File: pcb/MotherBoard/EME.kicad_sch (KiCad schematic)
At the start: 58 parts, among them J1 BMP180, J10 Reset, J11 UART2, J12 SPI_CONN, J13 UART0, J14 GPIO's, J17 Anemómetro, J19 I2C, J2 volti, J20 Jumper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

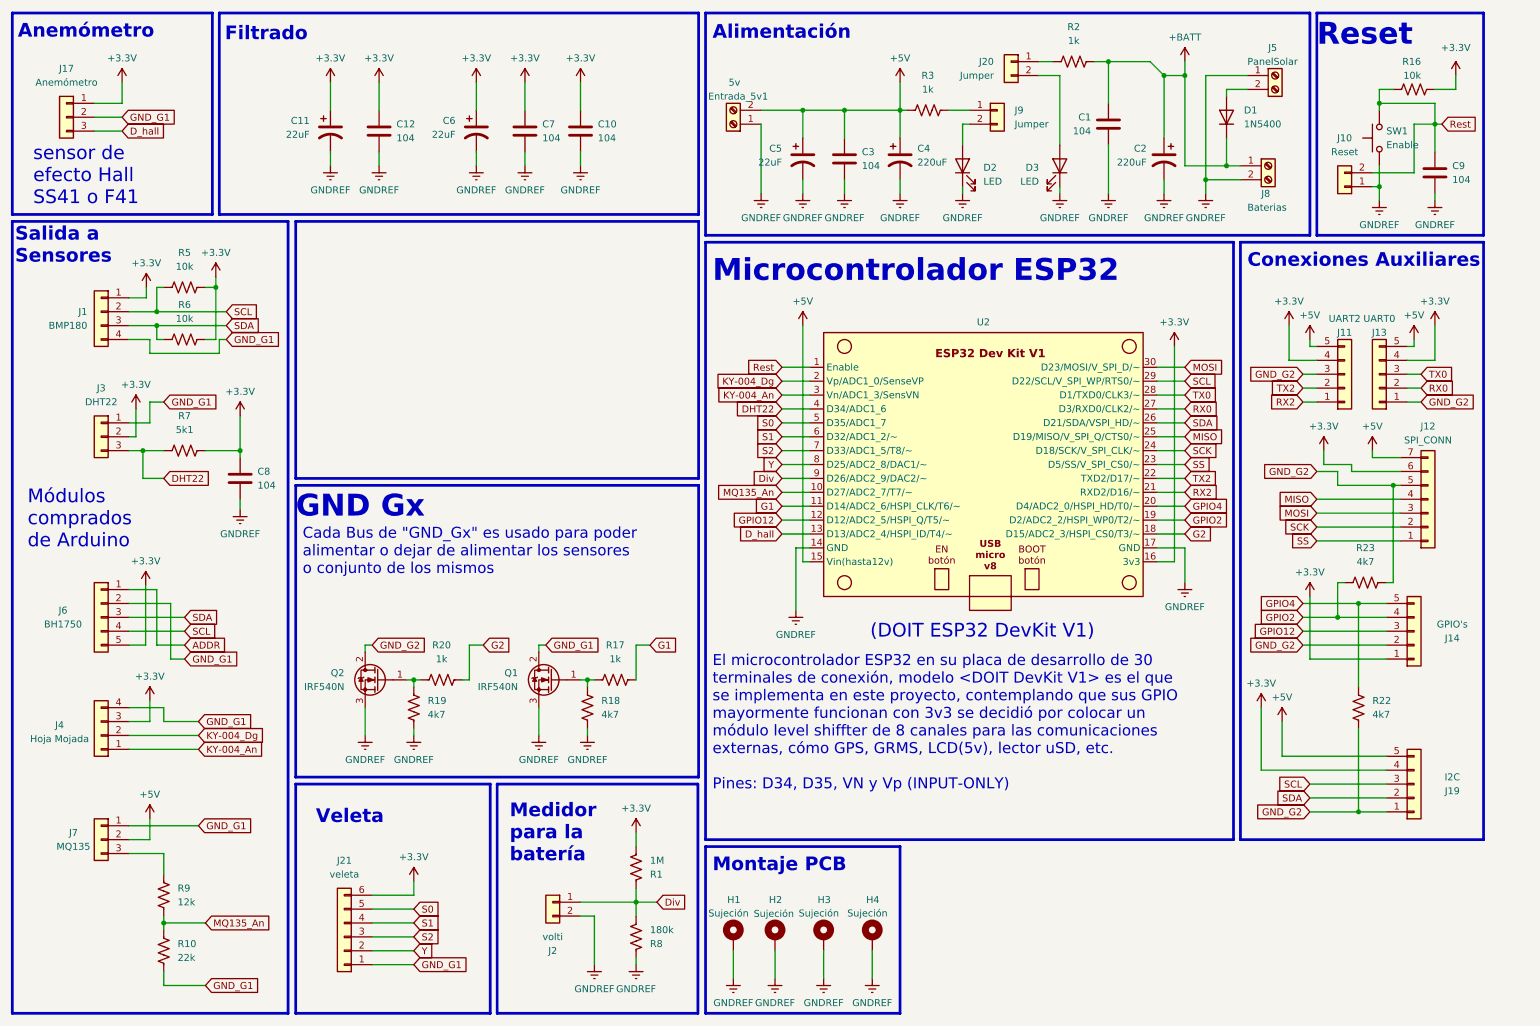
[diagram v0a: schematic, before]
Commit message: "se modificó conexión del DHT22 a otro pin, se agregó jumper G-g1 y g2, también conectores para extraer alimentación"
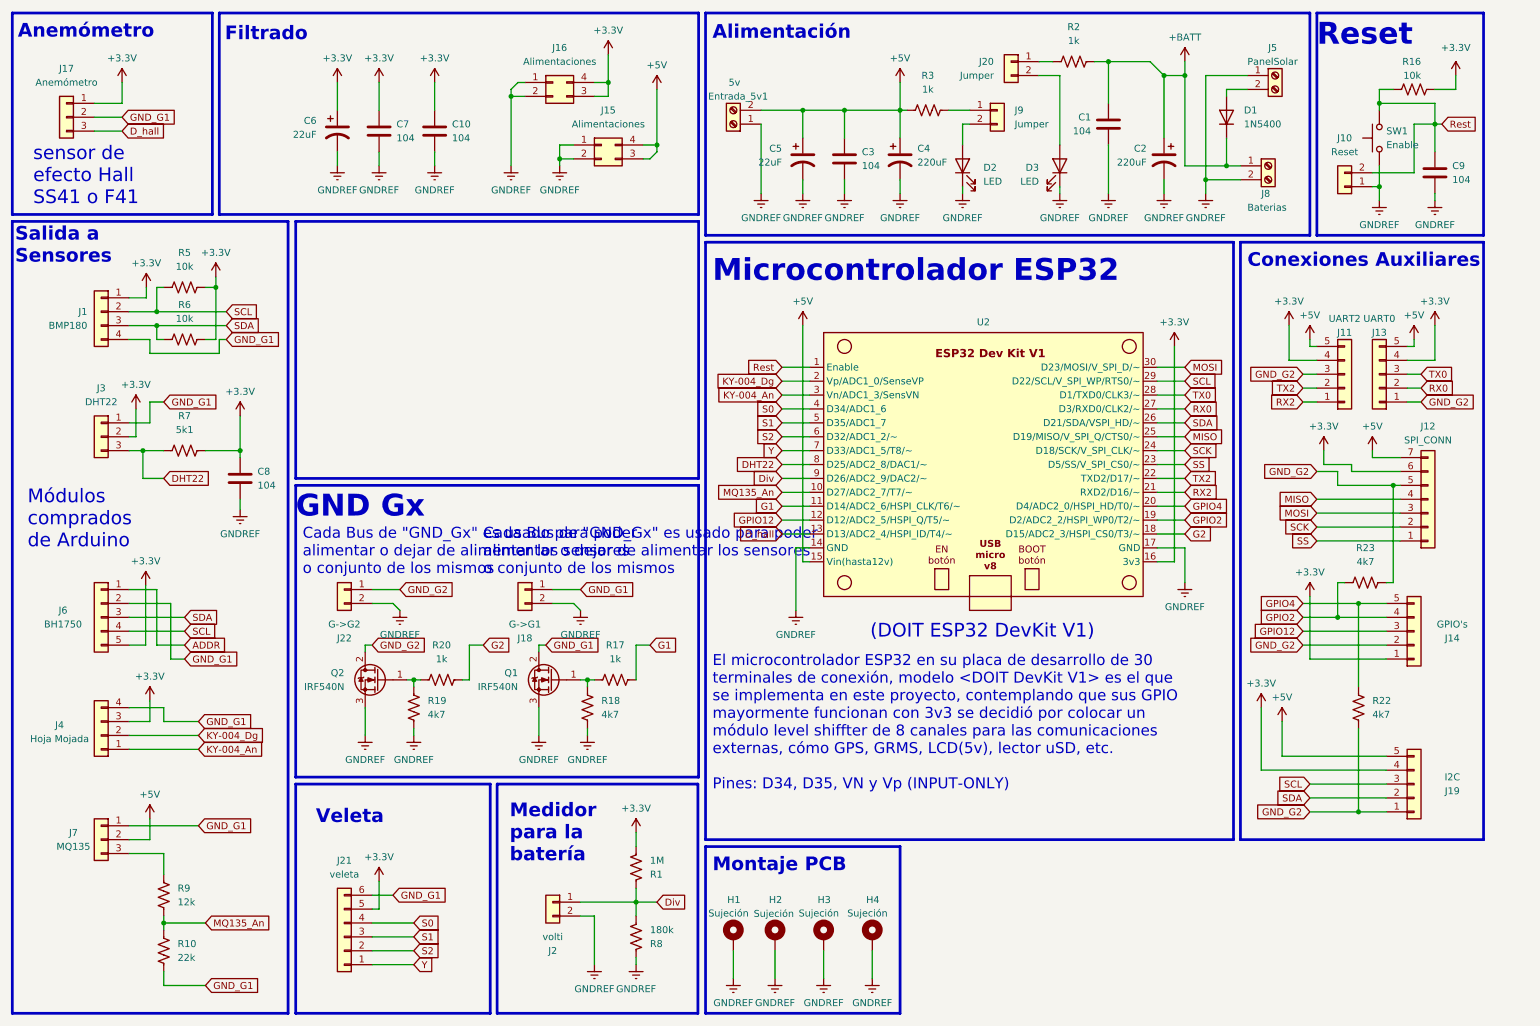
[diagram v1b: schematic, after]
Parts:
- removed C11: 22uF, Capacitor_THT:C_Radial_D8.0mm_H7.0mm_P3.50mm, symbol Device:C_Polarized_US
- removed C12: 104, Capacitor_THT:C_Disc_D7.0mm_W2.5mm_P5.00mm, symbol Device:C
- added J15, J16: Alimentaciones, Connector_PinHeader_2.54mm:PinHeader_2x02_P2.54mm_Vertical, symbol Connector_Generic:Conn_02x02_Counter_Clockwise
- added J18: G->G1, Connector_PinHeader_2.54mm:PinHeader_1x02_P2.54mm_Vertical, symbol Connector_Generic:Conn_01x02
- added J22: G->G2, Connector_PinHeader_2.54mm:PinHeader_1x02_P2.54mm_Vertical, symbol Connector_Generic:Conn_01x02
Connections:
- net +3.3V: now also J21.5 (Pin_5), J16.3 (Pin_3), J16.4 (Pin_4); no longer J21.6 (Pin_6)
- net +5V: now also J15.3 (Pin_3), J15.4 (Pin_4)
- net DHT22: now also U2.8 (D25/ADC2_8/DAC1/~); no longer U2.4 (D34/ADC1_6)
- net GNDREF: now also J15.1 (Pin_1), J15.2 (Pin_2), J16.1 (Pin_1), J16.2 (Pin_2), J18.2 (Pin_2), J22.2 (Pin_2)
- net GND_G1: now also J21.6 (Pin_6), J18.1 (Pin_1); no longer J21.1 (Pin_1)
- net GND_G2: now also J22.1 (Pin_1)
- net S0: now also J21.4 (Pin_4), U2.4 (D34/ADC1_6); no longer J21.5 (Pin_5), U2.5 (D35/ADC1_7)
- net S1: now also J21.3 (Pin_3), U2.5 (D35/ADC1_7); no longer J21.4 (Pin_4), U2.6 (D32/ADC1_2/~)
- net S2: now also J21.2 (Pin_2), U2.6 (D32/ADC1_2/~); no longer J21.3 (Pin_3), U2.7 (D33/ADC1_5/T8/~)
- net Y: now also J21.1 (Pin_1), U2.7 (D33/ADC1_5/T8/~); no longer J21.2 (Pin_2), U2.8 (D25/ADC2_8/DAC1/~)
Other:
- moved on the sheet: C10, C6, C7
